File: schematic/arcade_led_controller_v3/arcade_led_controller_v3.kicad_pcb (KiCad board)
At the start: 2 copper layers, 92.5 x 70 mm, 48 parts, among them J4 Pico_Socket_Row_2, J5 Pico_Socket_Row_1, Q1 Q_NMOS_GDS, Q2 Q_NMOS_GDS, Q3 Q_NMOS_GDS, Q4 Q_NMOS_GDS, Q5 Q_NMOS_GDS, Q6 Q_NMOS_GDS, Q7 Q_NMOS_GDS, Q8 Q_NMOS_GDS, U1 74AHCT125, U2 74AHCT125

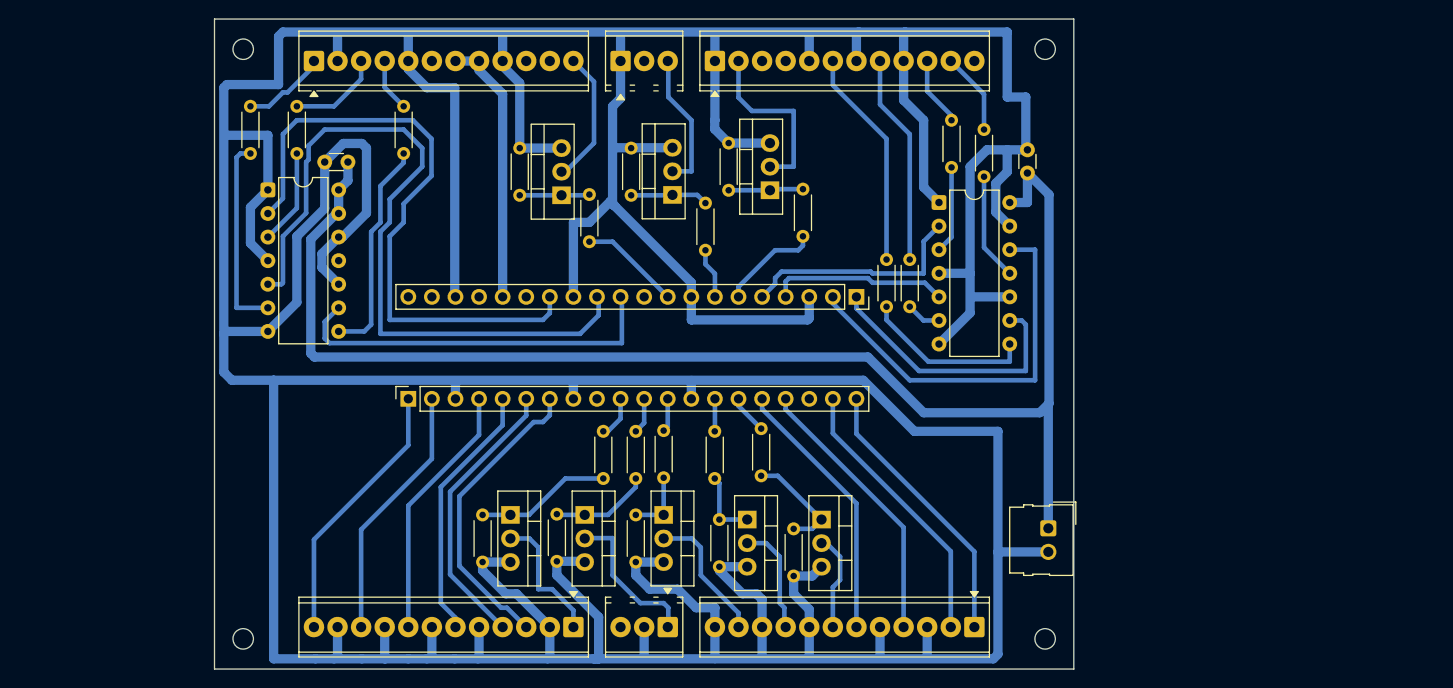
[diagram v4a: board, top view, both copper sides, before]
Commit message: convert to SMD resistors, MOSFETs, and capacitors
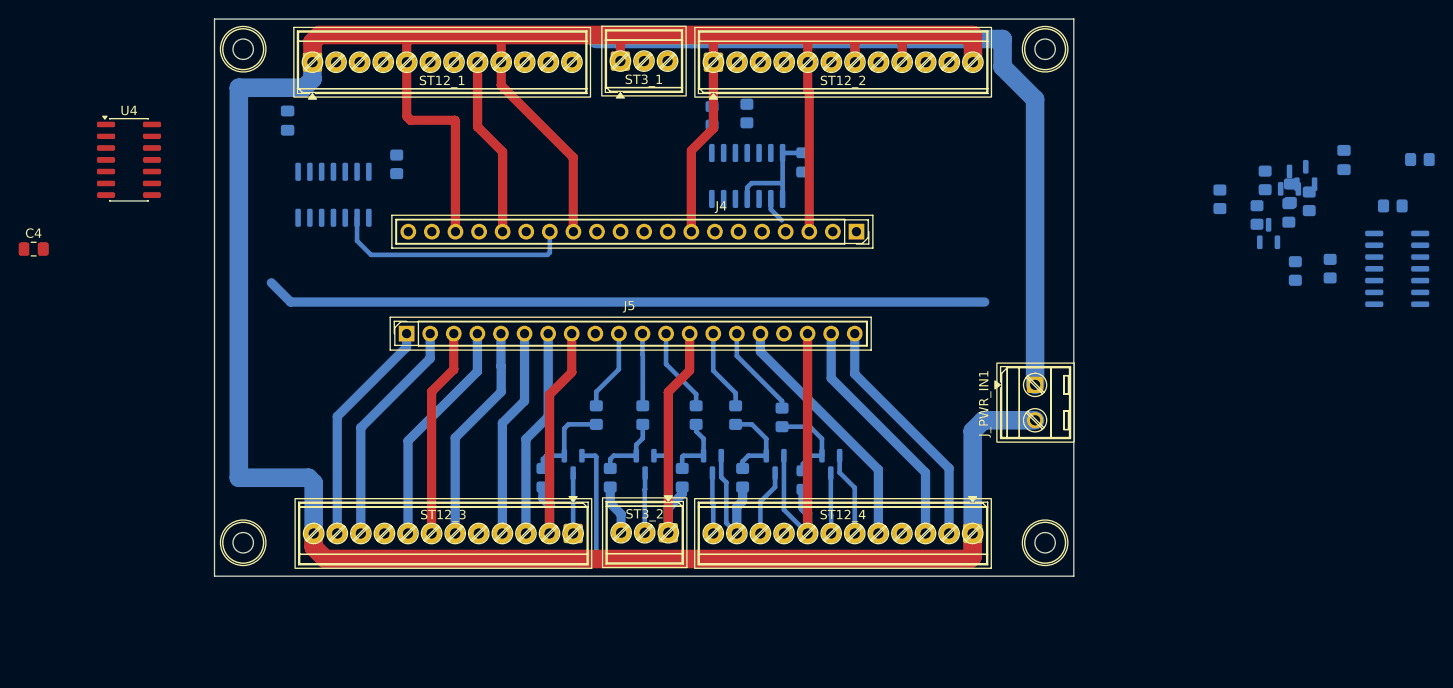
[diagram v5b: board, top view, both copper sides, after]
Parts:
- removed ST_IN_01x5, ST_OUT_01x5: Screw_Terminal_01x05, TerminalBlock_Phoenix:TerminalBlock_Phoenix_MPT-0,5-3-2.54_1x03_P2.54mm_Horizontal
- added C3: C, Capacitor_SMD:C_0805_2012Metric_Pad1.18x1.45mm_HandSolder, B.Cu at (114.0, 77.5)
- added C4: C, Capacitor_SMD:C_0805_2012Metric_Pad1.18x1.45mm_HandSolder, F.Cu at (86.7, 91.4)
- added ST3_1: Screw_Terminal_01x05, TerminalBlock_TE-Connectivity:TerminalBlock_TE_282834-3_1x03_P2.54mm_Horizontal, F.Cu at (149.8, 71.1)
- added ST3_2: Screw_Terminal_01x05, TerminalBlock_TE-Connectivity:TerminalBlock_TE_282834-3_1x03_P2.54mm_Horizontal, F.Cu at (155.0, 121.9)
- added U3: 74AHCT125, Package_SO:SOIC-14_3.9x8.7mm_P1.27mm, B.Cu at (118.9, 85.5)
- added U4: 74AHCT125, Package_SO:SOIC-14_3.9x8.7mm_P1.27mm, F.Cu at (96.9, 81.8)
- C1, C2: footprint Capacitor_THT:C_Disc_D3.0mm_W1.6mm_P2.50mm -> Capacitor_SMD:C_0805_2012Metric_Pad1.18x1.45mm_HandSolder; moved to B.Cu
- J_PWR_IN1: footprint Connector_Molex:Molex_SL_171971-0002_1x02_P2.54mm_Vertical -> TerminalBlock_MetzConnect:TerminalBlock_MetzConnect_Type086_RT03402HBLC_1x02_P3.81mm_Horizontal
- Q1, Q2, Q3, Q4, Q5, Q6, Q7, Q8: footprint Package_TO_SOT_THT:TO-220-3_Vertical -> Package_TO_SOT_SMD:SOT-23; moved to B.Cu
- R100k_1, R100k_2, R100k_3, R100k_4, R100k_5, R100k_6, R100k_7, R100k_8, R220_1, R220_2, R220_3, R220_4, R220_5, R220_6, R220_7, R220_8, R330[1]1, R330[1]2, R330[2]1, R330[3]2, R330[3]3, R330[4]1, R330[4]2: footprint Resistor_THT:R_Axial_DIN0204_L3.6mm_D1.6mm_P5.08mm_Horizontal -> Resistor_SMD:R_0805_2012Metric_Pad1.20x1.40mm_HandSolder; moved to B.Cu
- ST12_1: renamed from ST_OUT_01x12_1; footprint TerminalBlock_Phoenix:TerminalBlock_Phoenix_MPT-0,5-12-2.54_1x12_P2.54mm_Horizontal -> TerminalBlock_TE-Connectivity:TerminalBlock_TE_1-282834-2_1x12_P2.54mm_Horizontal
- ST12_2: renamed from ST_OUT_01x12_2; footprint TerminalBlock_Phoenix:TerminalBlock_Phoenix_MPT-0,5-12-2.54_1x12_P2.54mm_Horizontal -> TerminalBlock_TE-Connectivity:TerminalBlock_TE_1-282834-2_1x12_P2.54mm_Horizontal
- ST12_3: renamed from ST_IN_01x1_1; footprint TerminalBlock_Phoenix:TerminalBlock_Phoenix_MPT-0,5-12-2.54_1x12_P2.54mm_Horizontal -> TerminalBlock_TE-Connectivity:TerminalBlock_TE_1-282834-2_1x12_P2.54mm_Horizontal
- ST12_4: renamed from ST_IN_01x1_2; footprint TerminalBlock_Phoenix:TerminalBlock_Phoenix_MPT-0,5-12-2.54_1x12_P2.54mm_Horizontal -> TerminalBlock_TE-Connectivity:TerminalBlock_TE_1-282834-2_1x12_P2.54mm_Horizontal
- U1, U2: footprint Package_DIP:DIP-14_W7.62mm -> Package_SO:SOIC-14_3.9x8.7mm_P1.27mm; moved to B.Cu
- moved R100k_1 85.0 mm to (224.0, 86.2), turned to -90 degrees
- moved Q1 76.3 mm to (219.6, 89.7)
- moved R220_1 72.0 mm to (218.4, 87.7), turned to -90 degrees
- moved R100k_2 71.0 mm to (222.0, 85.4), turned to -90 degrees
- moved Q2 66.5 mm to (221.9, 84.0)
- moved R220_2 60.7 mm to (219.3, 84.0), turned to -90 degrees
- moved R100k_3 60.4 mm to (221.8, 87.5), turned to -90 degrees
- moved Q3 57.7 mm to (223.6, 83.5)
- moved R330[3]2 53.6 mm to (163.5, 76.8)
- moved U1 51.6 mm to (163.5, 83.5), turned to 90 degrees
- moved C1 51.5 mm to (169.5, 82.0), turned to 90 degrees
- moved R330[4]2 50.4 mm to (235.9, 81.7), turned to 0 degrees
- moved U2 49.9 mm to (233.5, 93.5), turned to 180 degrees
- moved R330[1]1 45.5 mm to (226.3, 93.5), turned to -90 degrees
- moved R220_3 45.1 mm to (214.4, 86.0), turned to -90 degrees
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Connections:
- J4 pad 27: /P1_DP_GP -> /3A(2)
- J4 pad 29: /P1_RS_GP -> /4A(2)
- J4 pad 31: /3A(2) -> unconnected-(J4-GP26-Pad31)
- J4 pad 32: /2A(2) -> unconnected-(J4-GP27-Pad32)
- J4 pad 34: /1A(2) -> /3A(3)
- Q1 pad 2: /P1_RS_CATHODE -> GND
- Q1 pad 3: GND -> /P1_RS_CATHODE
- Q2 pad 2: /P1_DP_CATHODE -> GND
- Q2 pad 3: GND -> /P1_DP_CATHODE
- Q3 pad 2: /P1_LS_CATHODE -> GND
- Q3 pad 3: GND -> /P1_LS_CATHODE
- Q4 pad 2: /REC_LED_CATHODE -> GND
- Q4 pad 3: GND -> /REC_LED_CATHODE
- Q5 pad 2: /P2_LS_CATHODE -> GND
- Q5 pad 3: GND -> /P2_LS_CATHODE
- Q6 pad 2: /P2_DP_CATHODE -> GND
- Q6 pad 3: GND -> /P2_DP_CATHODE
- Q7 pad 2: /P2_RS_CATHODE -> GND
- Q7 pad 3: GND -> /P2_RS_CATHODE
- Q8 pad 2: /PWR_LED_CATHODE -> GND
- Q8 pad 3: GND -> /PWR_LED_CATHODE
- R330[1]2 pad 1: /1Y(2) -> /3Y(3)
- R330[3]2 pad 1: /2Y(2) -> /4Y(2)
- ST12_1 pad 1: /P2_JOYSTICK_DATA -> GND
- ST12_1 pad 12: /P1_RS_CATHODE -> unconnected-(ST12_1-Pin_12-Pad12)
- ST12_1 pad 2: GND -> unconnected-(ST12_1-Pin_2-Pad2)
- ST12_1 pad 3: /ROTARY_LED_DATA -> unconnected-(ST12_1-Pin_3-Pad3)
- ST12_1 pad 4: /P2_BUTTON_DATA -> /ROTARY_LED_DATA
- ST12_2 pad 12: unconnected-(ST_OUT_01x12_2-Pin_12-Pad12) -> GND
- ST12_2 pad 2: /P1_LS_CATHODE -> /P1_RS_CATHODE
- ST12_2 pad 3: unconnected-(ST_OUT_01x12_2-Pin_3-Pad3) -> /P1_DP_CATHODE
- ST12_2 pad 4: unconnected-(ST_OUT_01x12_2-Pin_4-Pad4) -> /P1_LS_CATHODE
- ST12_3 pad 11: GND -> /DISPLAY_CS
- ST12_3 pad 12: /DISPLAY_CS -> GND
- ST12_4 pad 1: /DISPLAY_RST -> GND
- ST12_4 pad 10: GND -> /P2_RS_CATHODE
- ST12_4 pad 11: /P2_DP_CATHODE -> GND
- ST12_4 pad 12: GND -> /P2_DP_CATHODE
- ST12_4 pad 2: /ROTARY_CLK -> /DISPLAY_RST
- ST12_4 pad 3: GND -> /ROTARY_CLK
- ST12_4 pad 4: /ROTARY_DT -> GND
- ST12_4 pad 5: GND -> /ROTARY_DT
- ST12_4 pad 9: /P2_RS_CATHODE -> unconnected-(ST12_4-Pin_9-Pad9)
- U1 pad 1: GND -> +5V
- U1 pad 12: GND -> /4A(2)
- U1 pad 13: +5V -> GND
- U1 pad 2: /1A(2) -> GND
- U1 pad 4: GND -> +5V
- U1 pad 5: /2A(2) -> GND
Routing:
- net GND: track 745.3 -> 509.8 mm
- net /2A(2): track 79.7 -> 0.00 mm
- net /1A(2): track 67.3 -> 0.00 mm
- net /4A: track 42.7 -> 0.00 mm
- net /3A(2): track 41.2 -> 0.03 mm
- net /ROTARY_DT: track 29.8 -> 0.00 mm
- net /3A: track 29.2 -> 0.00 mm
- net /3A(3): track 0.00 -> 26.2 mm
- net /1A: track 24.8 -> 0.00 mm
- net /P1_BUTTON_DATA: track 23.8 -> 0.00 mm
- net /3Y(2): track 23.7 -> 0.00 mm
- net +5V: track 149.2 -> 172.5 mm
- net /ACCENT_DATA: track 22.7 -> 0.00 mm
- net /2Y(2): track 21.3 -> 0.00 mm
- net /2A: track 19.2 -> 0.00 mm
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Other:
- board size 92.5 x 70 mm -> 92.5 x 60 mm

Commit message: complete routing
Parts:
- removed C4: C, Capacitor_SMD:C_0805_2012Metric_Pad1.18x1.45mm_HandSolder
- removed U4: 74AHCT125, Package_SO:SOIC-14_3.9x8.7mm_P1.27mm
- moved R100k_1 105.9 mm to (118.1, 89.2), turned to 180 degrees
- moved Q1 98.9 mm to (120.9, 83.4)
- moved R220_1 94.5 mm to (124.0, 85.3), turned to 90 degrees
- moved R330[2]1 85.8 mm to (147.6, 79.2), turned to 90 degrees
- moved R330[4]1 84.5 mm to (139.9, 75.9), turned to 0 degrees
- moved R330[4]2 56.5 mm to (179.6, 77.2), turned to 90 degrees
- moved Q2 56.3 mm to (165.9, 78.2)
- moved U2 53.7 mm to (180.8, 83.1), turned to -90 degrees
- moved R220_2 53.2 mm to (166.1, 86.1), turned to 0 degrees
- moved R100k_2 53.0 mm to (169.4, 79.0), turned to 90 degrees
- moved Q3 51.5 mm to (172.5, 77.6)
- moved R100k_3 47.4 mm to (175.5, 77.2), turned to 90 degrees
- moved R330[1]1 45.9 mm to (183.6, 76.5), turned to 0 degrees
- moved R220_3 42.8 mm to (171.7, 82.8), turned to 0 degrees
- moved C2 41.2 mm to (186.7, 84.9)
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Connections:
- J4 pad 21: /3A -> /2A
- J4 pad 22: /4A -> /1A
- J4 pad 24: /2A -> /P1_LS_GP
- J4 pad 25: /1A -> /P1_DP_GP
- J4 pad 26: /P1_LS_GP -> /P1_RS_GP
- J4 pad 31: unconnected-(J4-GP26-Pad31) -> /1A(2)
- J4 pad 32: unconnected-(J4-GP27-Pad32) -> /1A(3)
- J4 pad 34: /3A(3) -> /2A(3)
- J4 pad 36: /PICO_3V3_OUT -> GND
- R330[1]2 pad 1: /3Y(3) -> /1Y(2)
- R330[2]1 pad 1: /4Y -> /1Y(3)
- R330[4]1 pad 1: /3Y -> /2Y(3)
- ST12_1 pad 11: unconnected-(ST12_1-Pin_11-Pad11) -> /P1_BUTTON_DATA
- ST12_1 pad 12: unconnected-(ST12_1-Pin_12-Pad12) -> GND
- ST12_1 pad 2: unconnected-(ST12_1-Pin_2-Pad2) -> /P1_RS_CATHODE
- ST12_1 pad 4: /ROTARY_LED_DATA -> unconnected-(ST12_1-Pin_4-Pad4)
- ST12_1 pad 7: /PICO_3V3_OUT -> unconnected-(ST12_1-Pin_7-Pad7)
- ST12_1 pad 8: /PICO_3V3_OUT -> GND
- ST12_2 pad 10: /OPTIONS_LED_DATA -> GND
- ST12_2 pad 11: /P1_JOYSTICK_DATA -> /ACCENT_DATA
- ST12_2 pad 2: /P1_RS_CATHODE -> /P2_JOYSTICK_DATA
- ST12_2 pad 3: /P1_DP_CATHODE -> /P2_BUTTON_DATA
- ST12_2 pad 4: /P1_LS_CATHODE -> GND
- ST12_2 pad 5: GND -> /P1_DP_CATHODE
- ST12_2 pad 6: /P1_BUTTON_DATA -> GND
- ST12_2 pad 7: GND -> /P1_LS_CATHODE
- ST12_2 pad 8: /ACCENT_DATA -> GND
- ST12_2 pad 9: GND -> /OPTIONS_LED_DATA
- ST12_4 pad 4: GND -> /ROTARY_DT
- ST12_4 pad 5: /ROTARY_DT -> /ROTARY_SW
- ST12_4 pad 6: /ROTARY_SW -> GND
- ST3_1 pad 1: GND -> /P1_JOYSTICK_DATA
- ST3_1 pad 2: /P2_JOYSTICK_DATA -> GND
- ST3_1 pad 3: /P2_BUTTON_DATA -> /ROTARY_LED_DATA
- U1 pad 1: +5V -> GND
- U1 pad 2: GND -> /1A(2)
- U2 pad 10: GND -> +5V
- U2 pad 12: /4A -> GND
- U2 pad 13: GND -> +5V
- U2 pad 9: /3A -> GND
- U3 pad 1: +5V -> GND
- U3 pad 10: GND -> +5V
- U3 pad 2: GND -> /1A(3)
- U3 pad 4: +5V -> GND
- U3 pad 5: GND -> /2A(3)
- U3 pad 9: /3A(3) -> GND
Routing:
- net GND: track 509.8 -> 727.1 mm
- net /P1_RS_GP: track 0.00 -> 47.7 mm
- net /ROTARY_DT: track 0.00 -> 26.8 mm
- net /3A(3): track 26.2 -> 0.00 mm
- net /PICO_3V3_OUT: track 19.4 -> 0.00 mm
- net /2Y(3): track 0.00 -> 19.4 mm
- net +5V: track 172.5 -> 153.3 mm
- net /2A: track 0.00 -> 14.8 mm
- net /1A: track 0.00 -> 12.5 mm
- net /P1_RS_CATHODE: track 0.00 -> 11.9 mm
- net /P2_BUTTON_DATA: track 0.00 -> 10.8 mm
- net /P2_JOYSTICK_DATA: track 0.00 -> 10.6 mm
- net /1A(2): track 0.00 -> 10.2 mm
- net /P1_DP_GATE: track 0.00 -> 10.1 mm
- net /P1_RS_GATE: track 0.00 -> 9.10 mm
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
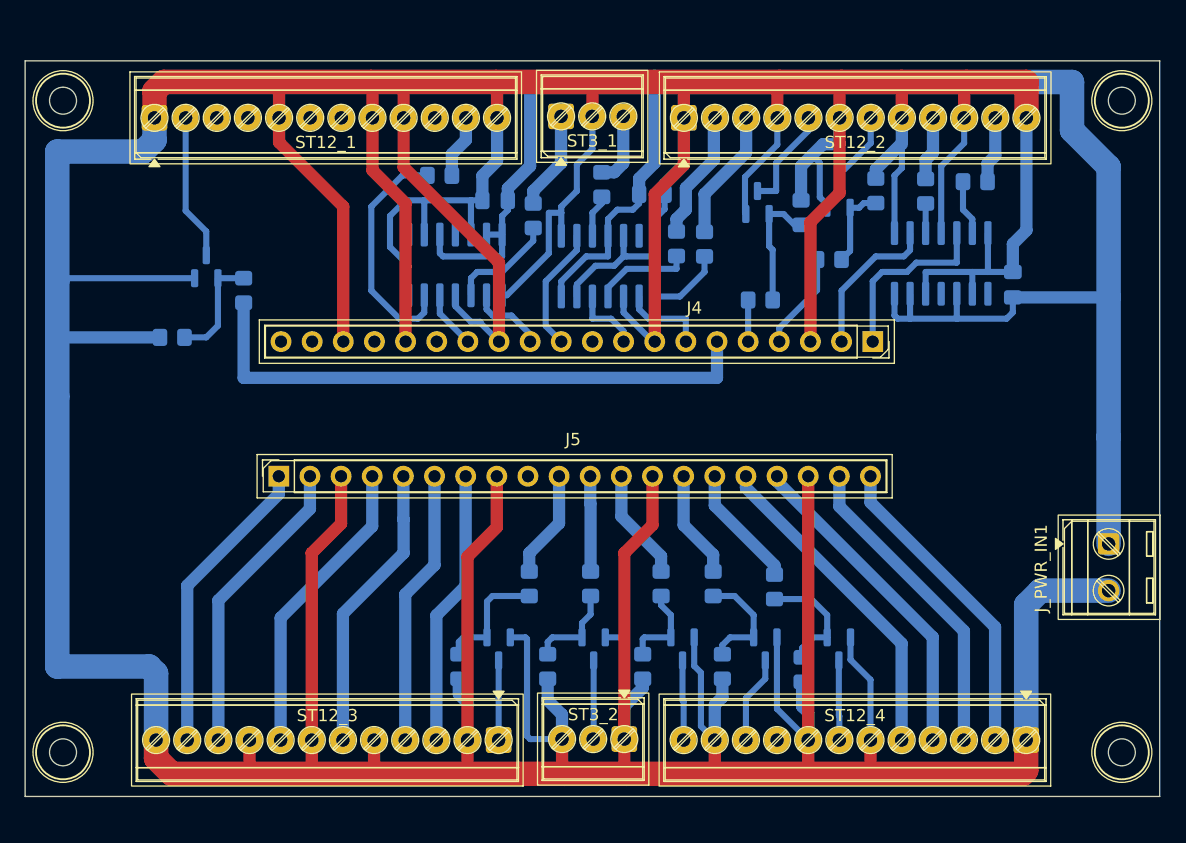
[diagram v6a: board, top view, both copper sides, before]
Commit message: Swap some screw terminals for jst connectors, and simplify routing
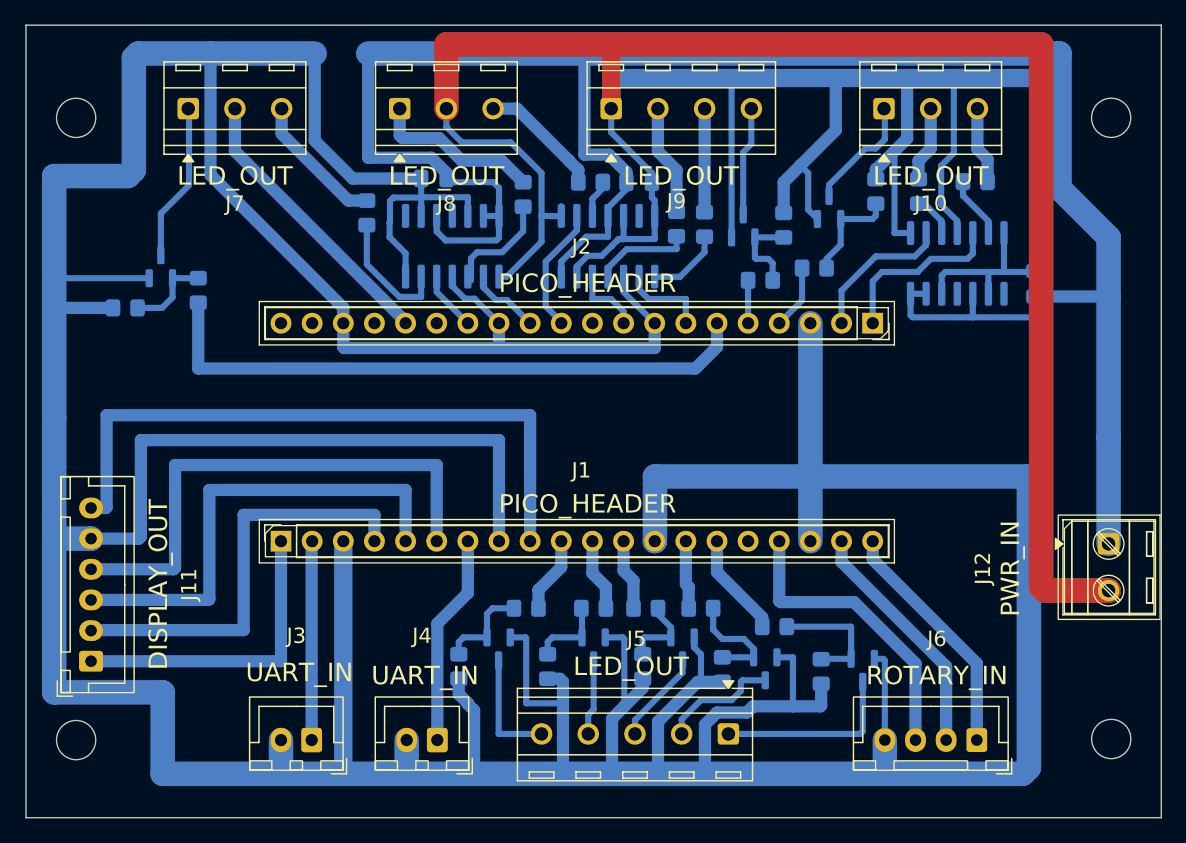
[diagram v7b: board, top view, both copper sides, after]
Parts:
- removed ST12_3, ST12_4: Screw_Terminal_01x12, TerminalBlock_TE-Connectivity:TerminalBlock_TE_1-282834-2_1x12_P2.54mm_Horizontal
- removed ST3_2: Screw_Terminal_01x05, TerminalBlock_TE-Connectivity:TerminalBlock_TE_282834-3_1x03_P2.54mm_Horizontal
- added J10: LED_OUT, TerminalBlock_MetzConnect:TerminalBlock_MetzConnect_Type086_RT03403HBLC_1x03_P3.81mm_Horizontal, F.Cu at (176.2, 70.5)
- added J11: DISPLAY_OUT, Connector_JST:JST_XH_B6B-XH-A_1x06_P2.50mm_Vertical, F.Cu at (111.5, 115.6)
- added J3: UART_IN, Connector_JST:JST_XH_B2B-XH-A_1x02_P2.50mm_Vertical, F.Cu at (129.5, 122.0)
- added J4: UART_IN, Connector_JST:JST_XH_B2B-XH-A_1x02_P2.50mm_Vertical, F.Cu at (139.8, 122.0)
- added J5: LED_OUT, TerminalBlock_MetzConnect:TerminalBlock_MetzConnect_Type086_RT03405HBLC_1x05_P3.81mm_Horizontal, F.Cu at (163.5, 121.5)
- added J6: ROTARY_IN, Connector_JST:JST_XH_B4B-XH-A_1x04_P2.50mm_Vertical, F.Cu at (183.8, 122.0)
- J1: renamed from J5; value Pico_Socket_Row_1 -> PICO_HEADER
- J12: renamed from J_PWR_IN1; value Conn_01x02 -> PWR_IN
- J2: renamed from J4; value Pico_Socket_Row_2 -> PICO_HEADER
- J7: renamed from ST12_1; value Screw_Terminal_01x12 -> LED_OUT; footprint TerminalBlock_TE-Connectivity:TerminalBlock_TE_1-282834-2_1x12_P2.54mm_Horizontal -> TerminalBlock_MetzConnect:TerminalBlock_MetzConnect_Type086_RT03403HBLC_1x03_P3.81mm_Horizontal
- J8: renamed from ST3_1; value Screw_Terminal_01x05 -> LED_OUT; footprint TerminalBlock_TE-Connectivity:TerminalBlock_TE_282834-3_1x03_P2.54mm_Horizontal -> TerminalBlock_MetzConnect:TerminalBlock_MetzConnect_Type086_RT03403HBLC_1x03_P3.81mm_Horizontal
- J9: renamed from ST12_2; value Screw_Terminal_01x12 -> LED_OUT; footprint TerminalBlock_TE-Connectivity:TerminalBlock_TE_1-282834-2_1x12_P2.54mm_Horizontal -> TerminalBlock_MetzConnect:TerminalBlock_MetzConnect_Type086_RT03404HBLC_1x04_P3.81mm_Horizontal
- REF** (x4): value MountingHole_2.2mm_M2 -> MountingHole_3.2mm_M3; footprint MountingHole:MountingHole_2.2mm_M2 -> MountingHole:MountingHole_3.2mm_M3
- moved J8 13.2 mm to (136.7, 70.5)
- moved R330[4]1 6.68 mm to (134.0, 79.0), turned to 90 degrees
- moved J9 5.98 mm to (153.9, 70.5)
- moved J1 5.30 mm to (127.0, 105.8)
- moved C3 5.30 mm to (139.5, 76.2)
- moved R100k_1 4.52 mm to (114.3, 86.8)
- moved Q1 3.70 mm to (117.2, 83.4)
- moved R220_1 3.70 mm to (120.2, 85.3)
- moved R220_8 3.25 mm to (167.2, 112.8), turned to 180 degrees
- moved J7 2.85 mm to (119.4, 70.5)
- moved Q8 2.62 mm to (174.4, 116.3)
- moved R220_6 2.36 mm to (156.8, 111.2), turned to 180 degrees
- moved R220_7 2.24 mm to (161.2, 111.2), turned to 180 degrees
- moved Q2 2.23 mm to (164.7, 80.1)
- moved R220_4 2.02 mm to (147.0, 111.2), turned to 0 degrees
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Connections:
- J1 pad 16: /ROTARY_SW -> unconnected-(J1-GP12-Pad16)
- J1 pad 17: /ROTARY_DT -> /ROTARY_SW
- J1 pad 19: /ROTARY_CLK -> /ROTARY_DT
- J1 pad 20: /DISPLAY_RST -> /ROTARY_CLK
- J1 pad 9: unconnected-(J5-GP6-Pad9) -> /DISPLAY_RST
- J2 pad 36: GND -> /PICO_3V3_OUT
- J7 pad 1: GND -> /P1_RS_CATHODE
- J7 pad 2: /P1_RS_CATHODE -> /PICO_3V3_OUT
- J7 pad 3: unconnected-(ST12_1-Pin_3-Pad3) -> /P1_BUTTON_DATA
- J9 pad 4: GND -> /P1_DP_CATHODE
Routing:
- net GND: track 727.1 -> 808.2 mm
- net /DISPLAY_RST: track 25.7 -> 53.6 mm
- net +5V: track 153.3 -> 177.1 mm
- net /PICO_3V3_OUT: track 0.00 -> 23.3 mm
- net /DISPLAY_DC: track 22.5 -> 42.8 mm
- net /DISPLAY_MOSI: track 23.6 -> 38.8 mm
- net /DISPLAY_SCK: track 24.6 -> 34.7 mm
- net /2Y(3): track 19.4 -> 10.4 mm
- net /PWR_LED_CATHODE: track 6.52 -> 15.1 mm
- net /P1_SIG: track 24.6 -> 16.2 mm
- net /ROTARY_DT: track 26.8 -> 19.8 mm
- net /P1_BUTTON_DATA: track 5.17 -> 11.3 mm
- net /ROTARY_CLK: track 25.7 -> 19.7 mm
- net /P1_JOYSTICK_DATA: track 8.44 -> 13.8 mm
- net /P2_SIG: track 22.5 -> 17.3 mm
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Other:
- board size 92.5 x 60 mm -> 92.6 x 64.6 mm
